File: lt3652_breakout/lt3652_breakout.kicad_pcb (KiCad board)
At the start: 2 copper layers, 55.2 x 50.3 mm, 38 parts, among them U1 LT3652

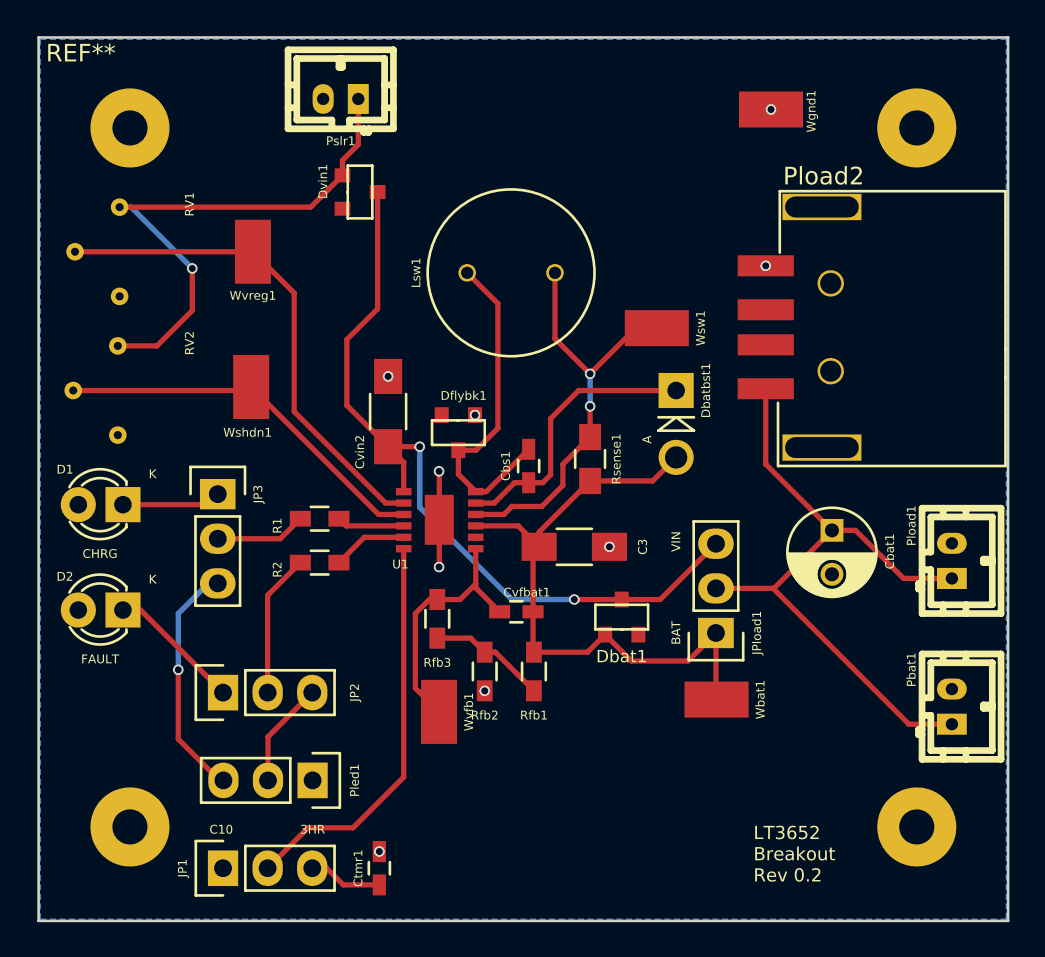
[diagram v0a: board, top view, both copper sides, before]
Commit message: Release of Rev 0.2 of the LT3652 breakout
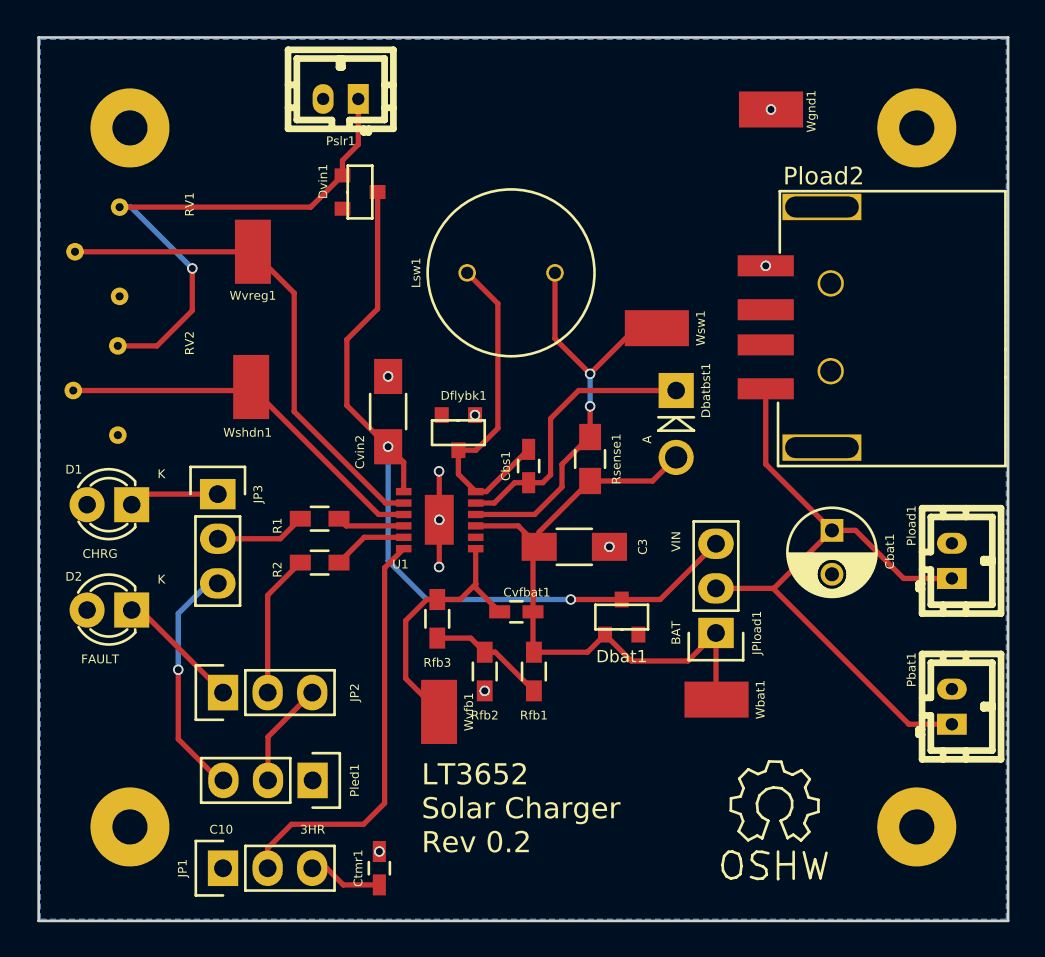
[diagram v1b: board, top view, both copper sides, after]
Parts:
- added ?: Symbol_OSHW-Logo_SilkScreen, Symbols:Symbol_OSHW-Logo_SilkScreen, F.Cu at (157.8, 115.0)
- moved D1 0.50 mm to (121.2, 97.8)
- moved D2 0.50 mm to (121.2, 103.8)
- renumbered REF** to ?
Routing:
- net /VIN: track 44.7 -> 46.5 mm
- net Net-(JP1-Pad2): track 22.9 -> 23.8 mm
- net /VFB: track 14.5 -> 15.0 mm
- net Net-(D2-Pad1): track 7.65 -> 7.15 mm
- net Net-(D1-Pad1): track 5.65 -> 5.15 mm
- net GND: track 5.46 -> 5.50 mm, vias 9 -> 10
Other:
- board text added: "LT3652 Solar Charger Rev 0.2"
- board text removed: "LT3652 Breakout Rev 0.2"

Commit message: Upload of Rev 0.3
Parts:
- added Pslr2: JST PH, w_conn_jst-ph:b2b-ph-kl, F.Cu at (143.6, 74.8)
- added Rshdn1: 10K, Resistors_SMD:R_0603_HandSoldering, F.Cu at (126.4, 91.2)
- added Rvrg1: 10K, Resistors_SMD:R_0603_HandSoldering, F.Cu at (126.4, 83.5)
- Dbatbst1: footprint Diodes_ThroughHole:Diode_DO-41_SOD81_Vertical_AnodeUp -> Diodes_ThroughHole:Diode_DO-35_SOD27_Horizontal_RM10
- R1, R2: value 220 -> 10K
- U1: footprint lt3652:LT3652MSE -> lt3652:LT3652MSE_HandSoldering
- moved ? 13.5 mm to (144.3, 115.7)
- moved Wbat1 6.62 mm to (160.9, 107.2)
- moved JPload1 4.49 mm to (155.4, 109.5)
- moved Wvreg1 2.70 mm to (130.2, 85.2)
- moved Wshdn1 2.20 mm to (130.2, 91.2)
- moved Dvin1 1.10 mm to (133.1, 80.0), turned to 180 degrees
- moved RV1 0.10 mm to (120.4, 83.5), turned to 180 degrees
- moved RV2 0.10 mm to (120.4, 91.2), turned to 180 degrees
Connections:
- D1 pad 2: GND -> /VIN
- D2 pad 2: GND -> /VIN
- Pbat1 pad 1: Net-(Cbat1-Pad1) -> /BAT
- Pled1 pad 1: GND -> /VIN
- RV1 pad 3: GND -> Net-(RV1-Pad3)
- RV2 pad 3: GND -> Net-(RV2-Pad3)
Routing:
- net /VIN: track 46.5 -> 88.6 mm
- net /BAT: track 36.5 -> 56.7 mm
- net Net-(Dvin1-Pad3): track 31.2 -> 44.9 mm, vias 1 -> 0
- net Net-(Cbat1-Pad1): track 39.2 -> 28.0 mm
- net /SENSE: track 24.2 -> 31.8 mm, vias 2 -> 0
- net GND: track 5.50 -> 11.0 mm, vias 10 -> 5
- net Net-(RV1-Pad3): track 0.00 -> 3.92 mm
- net Net-(RV2-Pad3): track 0.00 -> 3.88 mm
- net /SW: track 19.2 -> 21.3 mm
- net /VIN_REG: track 28.6 -> 26.6 mm
- net /VFB: track 15.0 -> 15.9 mm
- net Net-(JP1-Pad2): track 23.8 -> 23.0 mm
- net Net-(JP3-Pad3): track 13.7 -> 13.9 mm, vias 1 -> 0
- added copper zone on F.Cu, net GND
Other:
- board text added: "LT3652 Solar Charger Rev 0.3"
- board text added: "Url: https://github.com/malcolmspiteri/weatherstation/tree/master/lt3652_breakout Date: 06-03-2016"
- board text removed: "LT3652 Solar Charger Rev 0.2"
